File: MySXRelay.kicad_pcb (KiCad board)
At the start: 2 copper layers, 50 parts, among them K2 FH44L-1AT-L1-DC5V, Q1 2N7002, U1 MIC4427, U2 BL0942, U3 BP2525X, U4 Si8642BB-B-IS1

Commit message: finished schematic
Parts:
- C1, C13, C14: footprint Capacitor_SMD:C_0603_1608Metric -> Capacitor_SMD:C_0402_1005Metric
- C5: value 4.7u/400V -> 2.2u/400V; footprint Capacitor_THT:CP_Radial_D10.0mm_P5.00mm -> Capacitor_THT:CP_Radial_D8.0mm_P3.50mm
- C6: value 680u/10V -> 470u/10V
- L1: value 330m/300mA -> 330u; footprint Inductor_THT:L_Radial_D7.0mm_P3.00mm -> Inductor_SMD:L_1812_4532Metric_Pad1.30x3.40mm_HandSolder
- TH1: value 50mA -> ERF-LX005V2
- X1: moved to B.Cu
- moved X1 2.16 mm to (110.0, 65.0), turned to 180 degrees
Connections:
- X1 pad 1: VCC -> VRAW
- X1 pad 10: D3_INT -> D4_INT
- X1 pad 11: D6_PWM -> D5_PWM
- X1 pad 12: D5_PWM -> D6_PWM
- X1 pad 13: D8_SDA -> D7_SCL
- X1 pad 14: D7_SCL -> D8_SDA
- X1 pad 15: D10_A4 -> D9_A3
- X1 pad 16: D9_A3 -> D10_A4
- X1 pad 17: D12_MISO_RX -> D11_MOSI_TX
- X1 pad 18: D11_MOSI_TX -> D12_MISO_RX
- X1 pad 19: D14_CS -> D13_SCK
- X1 pad 2: VRAW -> VCC
- X1 pad 20: D13_SCK -> D14_CS
- X1 pad 3: GND -> VCCIO
- X1 pad 4: VCCIO -> GND
- X1 pad 5: D2_RX -> D1_TX
- X1 pad 6: D1_TX -> D2_RX
- X1 pad 7: LEGACY_ID -> RST
- X1 pad 8: RST -> LEGACY_ID
- X1 pad 9: D4_INT -> D3_INT

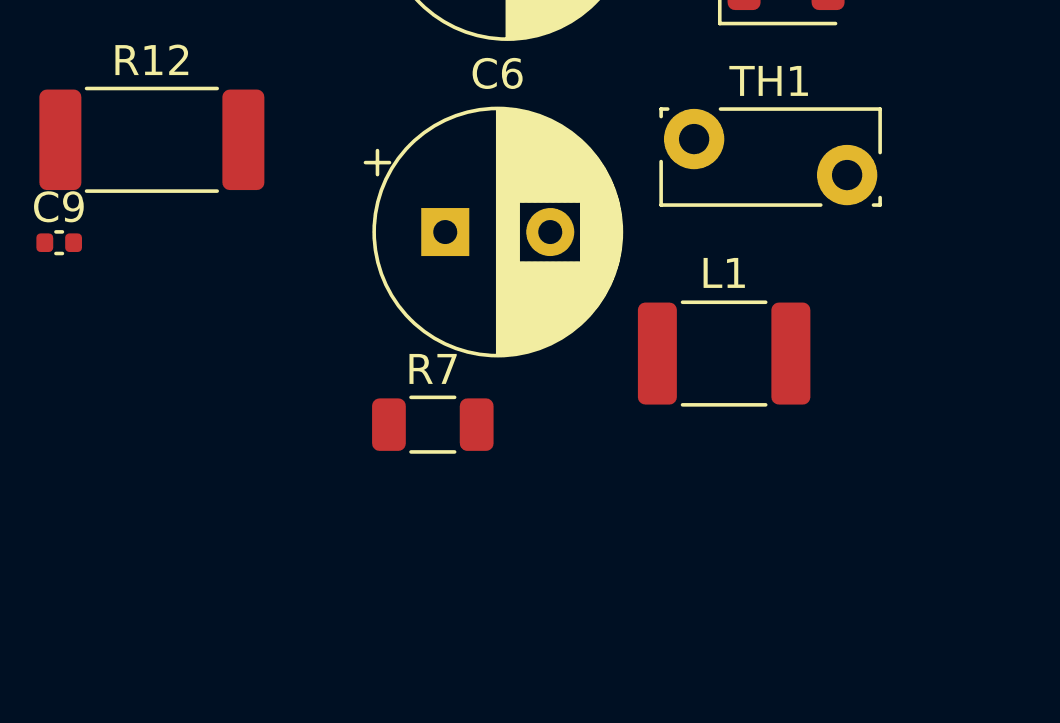
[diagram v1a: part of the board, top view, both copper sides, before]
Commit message: add LDO on mains power supply output
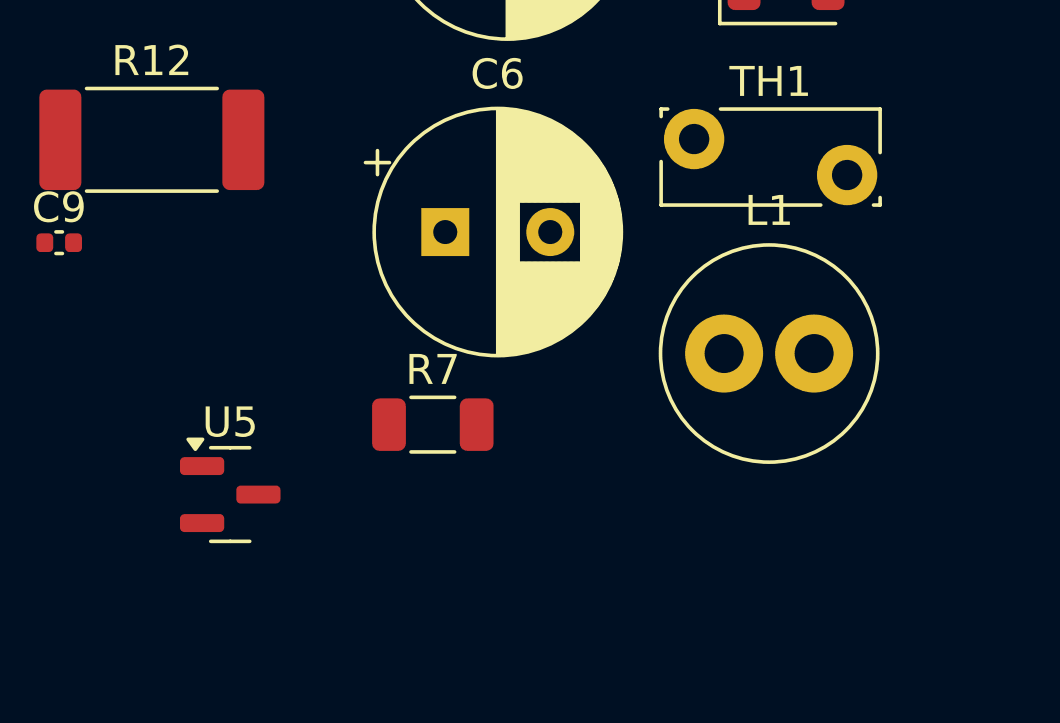
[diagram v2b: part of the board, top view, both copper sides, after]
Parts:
- added U5: MCP1703Ax-180xxTT, Package_TO_SOT_SMD:SOT-23, F.Cu at (118.2, 129.4)
- L1: footprint Inductor_SMD:L_1812_4532Metric_Pad1.30x3.40mm_HandSolder -> Inductor_THT:L_Radial_D7.0mm_P3.00mm
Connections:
- C6 pad 1: +3V3 -> Net-(U5-VI)
- L1 pad 2: +3V3 -> Net-(U5-VI)
- R8 pad 2: +3V3 -> Net-(U5-VI)
- R9 pad 1: +3V3 -> Net-(U5-VI)
- U3 pad 2: unconnected-(U3-SEL-Pad2) -> Net-(D6-K)

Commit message: setup PCS dimensions
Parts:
- K2, X2: moved to B.Cu
- moved K2 87.3 mm to (180.1, 125.8), turned to 90 degrees
- moved R12 54.4 mm to (166.2, 97.5)
- moved X2 50.2 mm to (176.9, 85.1), turned to -90 degrees
- moved TH1 49.0 mm to (164.3, 79.3)
- moved X1 45.9 mm to (136.8, 102.3)
- moved U4 44.8 mm to (156.1, 104.4)
- moved C5 44.6 mm to (164.4, 87.8)
- moved U2 44.0 mm to (165.4, 105.6)
- moved U1 43.7 mm to (165.6, 124.0)
- moved C6 39.5 mm to (147.3, 87.8)
- moved L1 37.5 mm to (155.8, 93.7)
- moved X3 37.4 mm to (143.8, 123.9)
- moved U3 33.0 mm to (158.1, 85.5)
- moved D7 21.5 mm to (132.8, 91.6)
- moved D5 14.8 mm to (138.6, 91.3)
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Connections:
- X2 pad 1: L_OUT -> N_IN
- X2 pad 2: L_IN -> N_OUT
- X2 pad 3: N_OUT -> L_IN
- X2 pad 4: N_IN -> L_OUT
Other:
- board outline added: 46.2 x 45.1 mm

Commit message: WIP
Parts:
- removed K2: FH44L-1AT-L1-DC5V, Relay_THT:Relay_SPST_Panasonic_ADW11
- added K1: FH44L-1AT-L1-DC5V, MySXRelay:RELAY-TH_FH44L-1AT-L1-DC5V, B.Cu at (172.0, 87.8)
- C5, C6, C7, D6, D7, L1, R7, R8, TH1: moved to B.Cu
- X2: footprint TerminalBlock_Phoenix:TerminalBlock_Phoenix_MKDS-1,5-4-5.08_1x04_P5.08mm_Horizontal -> MySXRelay:MSTB_2,5_4-G
- moved D1 48.1 mm to (158.1, 108.1)
- moved D2 48.1 mm to (158.1, 112.7)
- moved D3 48.1 mm to (158.1, 117.3)
- moved Q1 48.1 mm to (158.1, 122.0)
- moved C1 48.1 mm to (153.6, 106.9)
- moved C2 48.1 mm to (153.6, 109.5)
- moved R1 48.1 mm to (153.6, 112.0)
- moved R2 48.1 mm to (153.6, 114.5)
- moved R3 48.1 mm to (153.6, 117.0)
- moved R4 48.1 mm to (153.6, 119.5)
- moved R5 48.1 mm to (153.6, 122.0)
- moved R6 48.1 mm to (153.6, 124.5)
- moved U2 47.9 mm to (125.8, 78.7), turned to 90 degrees
- moved C9 43.5 mm to (152.3, 103.3)
- moved C11 43.5 mm to (143.2, 103.7)
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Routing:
- net L_OUT: track 0.00 -> 17.1 mm
- net Net-(D2-COM): track 0.00 -> 7.72 mm
- net Net-(D6-K): track 0.00 -> 5.40 mm
- net L_IN: track 0.00 -> 5.16 mm
- net Net-(D7-K): track 0.00 -> 3.64 mm
- net Net-(D7-A): track 0.00 -> 1.90 mm
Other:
- board size 46.2 x 45.1 mm -> 47.2 x 45.1 mm

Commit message: PCB WIP
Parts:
- C1, C10, C11, C12, C13, C14, C2, C3, C4, C8, C9, D1, D2, D3, D4, Q1, R1, R10, R11, R13, R2, R3, R4, R5, R6, R9, U1, U2, U3, U4, U5: moved to B.Cu
- moved C3 46.9 mm to (166.1, 123.9)
- moved C8 44.1 mm to (181.2, 121.2), turned to 90 degrees
- moved R9 40.1 mm to (178.2, 118.9)
- moved R18 36.0 mm to (169.8, 83.6), turned to 180 degrees
- moved R13 35.1 mm to (148.3, 84.0), turned to -90 degrees
- moved R17 30.6 mm to (165.2, 83.6), turned to 180 degrees
- moved U5 29.9 mm to (178.4, 121.3), turned to 180 degrees
- moved R7 26.5 mm to (178.2, 97.2), turned to 90 degrees
- moved R16 25.4 mm to (160.6, 83.6), turned to 180 degrees
- moved U2 25.4 mm to (148.1, 90.7), turned to 0 degrees
- moved L1 25.2 mm to (178.8, 104.2)
- moved R10 25.2 mm to (157.7, 93.2), turned to -90 degrees
- moved U4 25.0 mm to (150.1, 100.5), turned to -90 degrees
- moved R11 24.9 mm to (152.8, 93.3), turned to -90 degrees
- moved D6 24.7 mm to (179.2, 100.8), turned to 0 degrees
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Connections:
- D3 pad 2: VCCIO -> VCC
- D4 pad 1: VCCIO -> VCC
- K1 pad 13: L_IN -> L_OUT
- K1 pad 14: L_OUT -> L_IN
- X1 pad 3: VCCIO -> VCC
- X2 pad 3: L_IN -> L_OUT
- X2 pad 4: L_OUT -> L_IN
- X3 pad 1: VCCIO -> VCC
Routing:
- net GND: track 0.00 -> 104.3 mm
- net VCC: track 0.00 -> 68.1 mm, vias 0 -> 3
- net D5_PWM: track 0.00 -> 37.2 mm, vias 0 -> 2
- net D11_MOSI_TX: track 0.00 -> 29.1 mm, vias 0 -> 1
- net SW: track 0.00 -> 24.2 mm, vias 0 -> 1
- net D12_MISO_RX: track 0.00 -> 24.0 mm, vias 0 -> 1
- net Net-(D1-COM): track 0.00 -> 21.3 mm, vias 0 -> 2
- net D3_INT: track 0.00 -> 17.6 mm, vias 0 -> 1
- net LED: track 0.00 -> 13.6 mm
- net L_OUT: track 17.1 -> 6.76 mm
- net D4_INT: track 0.00 -> 9.18 mm
- net N_IN: track 0.00 -> 6.84 mm, vias 0 -> 1
- net Net-(Q1-G): track 0.00 -> 6.08 mm
- net Net-(D6-K): track 5.40 -> 0.00 mm
- net Net-(U1-IN_B): track 0.00 -> 5.13 mm
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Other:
- outline, holes or cut-outs redrawn

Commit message: WIP PCB
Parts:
- moved R11 5.86 mm to (158.7, 92.9)
- moved R10 4.86 mm to (152.8, 92.9)
- moved C5 1.17 mm to (176.4, 89.1)
- moved D5 1.17 mm to (178.5, 86.8)
- moved C9 0.58 mm to (144.7, 87.4), turned to 90 degrees
- moved C11 0.57 mm to (157.2, 95.2)
- moved C10 0.45 mm to (153.9, 95.2)
- moved C13 0.33 mm to (145.9, 96.3)
- turned R12 to 180 degrees
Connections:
- X2 pad 1: N_IN -> N_OUT
- X2 pad 2: N_OUT -> N_IN
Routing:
- net N_IN: track 6.84 -> 113.2 mm, vias 1 -> 5
- net +3V3: track 0.00 -> 69.3 mm, vias 0 -> 2
- net Net-(U5-VI): track 0.00 -> 16.3 mm
- net Net-(U2-IN): track 0.00 -> 15.1 mm
- net CF1: track 0.00 -> 12.5 mm
- net Net-(D6-K): track 0.00 -> 10.9 mm
- net Net-(U2-IP): track 0.00 -> 10.2 mm
- net Net-(D5-K): track 0.00 -> 10.1 mm, vias 0 -> 1
- net L_IN: track 4.30 -> 12.8 mm
- net Net-(U2-VP): track 0.00 -> 8.00 mm, vias 0 -> 1
- net RX: track 0.00 -> 6.15 mm
- net TX: track 0.00 -> 6.04 mm
- net Net-(D7-K): track 0.00 -> 3.78 mm
- net Net-(D7-A): track 0.00 -> 3.17 mm
- net Net-(D5-A): track 0.00 -> 2.52 mm
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- added copper zone on B.Cu, net Net-(D5-K)
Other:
- outline, holes or cut-outs redrawn

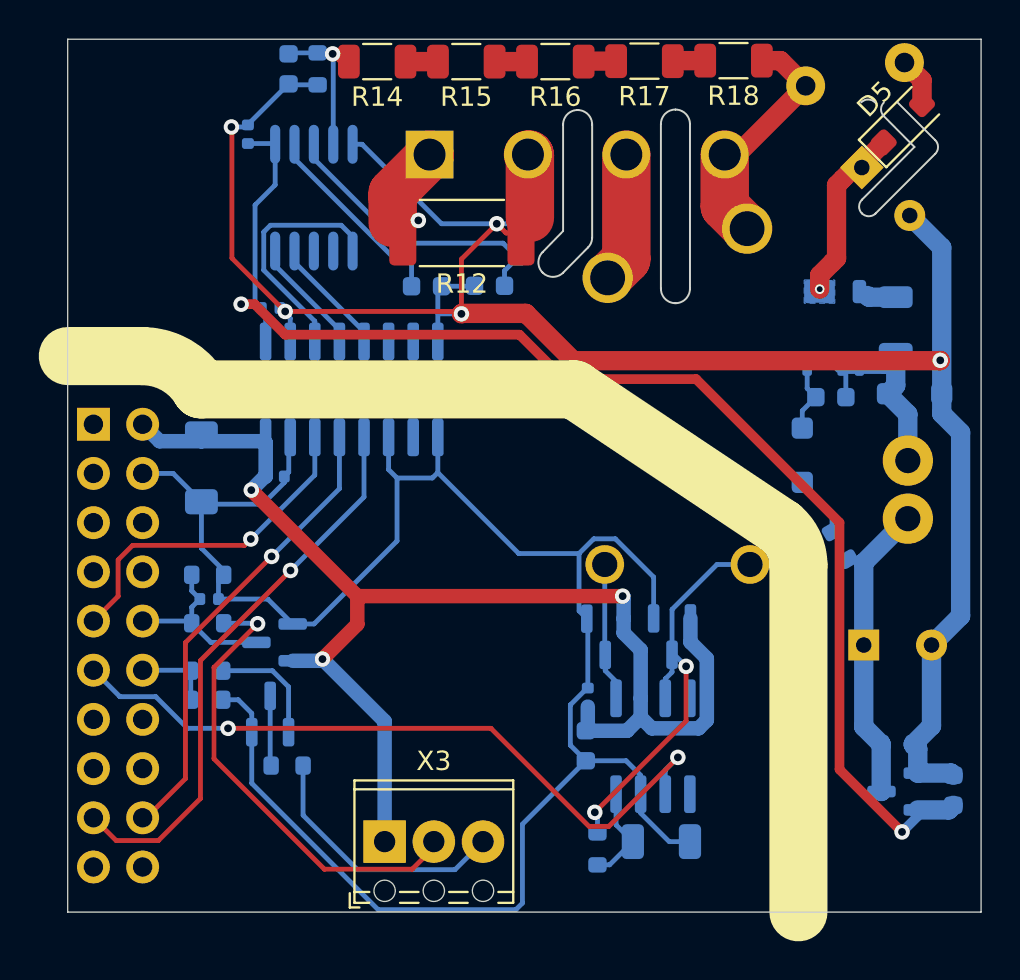
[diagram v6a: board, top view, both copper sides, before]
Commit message: PCB placment and routing finished
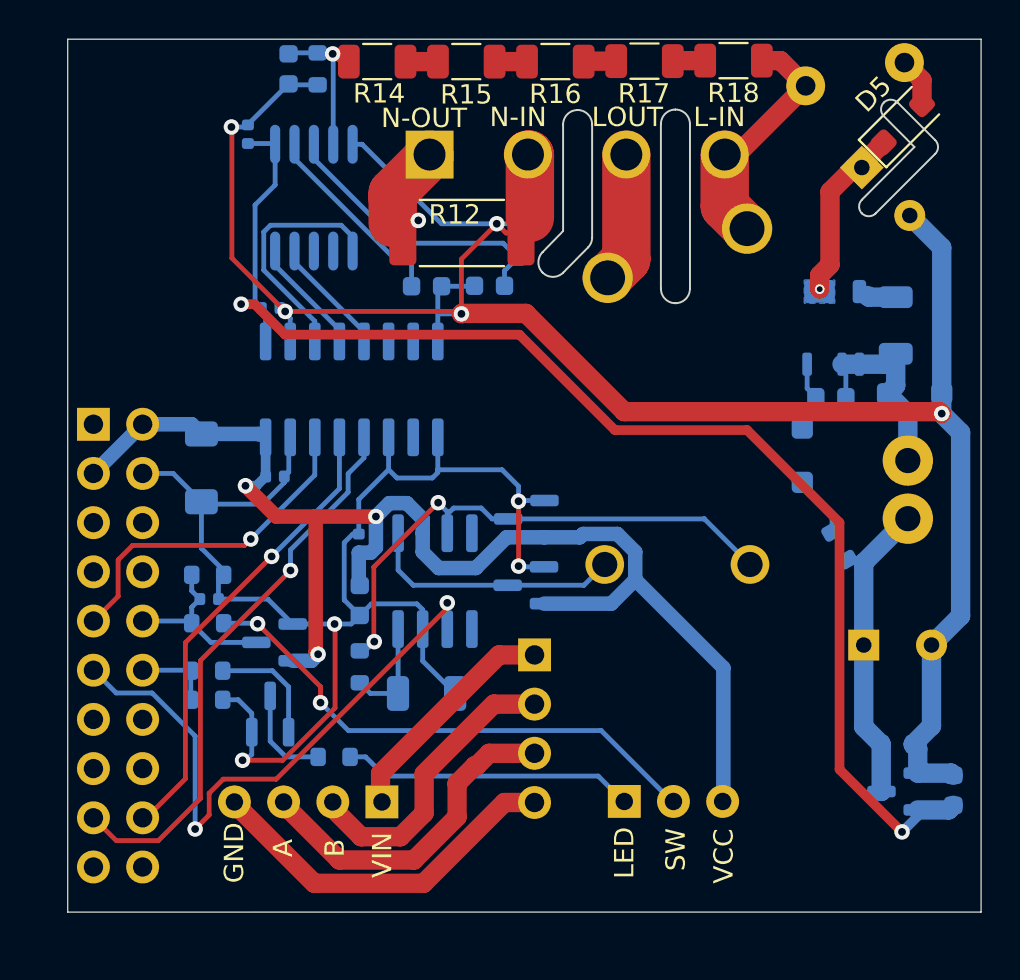
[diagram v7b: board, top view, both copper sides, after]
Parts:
- added X4: ~, Connector_PinSocket_2.54mm:PinSocket_1x04_P2.54mm_Vertical, B.Cu at (159.5, 114.3)
- added X5: ~, MySXRelay:JST-XH_S_4P-2.54MM-PIN1-RIGHT, B.Cu at (154.2, 121.9)
- X3: footprint TerminalBlock_Phoenix:TerminalBlock_Phoenix_MPT-0,5-3-2.54_1x03_P2.54mm_Horizontal -> MySXRelay:JST-XH_S_3P-2.54MM; moved to B.Cu
- moved R1 15.5 mm to (150.5, 114.9)
- moved X3 15.1 mm to (166.7, 121.8), turned to -90 degrees
- moved C3 14.3 mm to (153.9, 116.2)
- moved C1 14.2 mm to (150.4, 108.5)
- moved U1 14.1 mm to (154.4, 110.5)
- moved C2 13.9 mm to (150.5, 111.5)
- moved D1 9.67 mm to (159.1, 107.2), turned to 180 degrees
- moved D2 4.89 mm to (159.1, 110.7), turned to 180 degrees
- moved R5 2.47 mm to (149.2, 119.5)
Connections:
- X3 pad 1: VCC -> LED
- X3 pad 3: LED -> VCC
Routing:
- net GND: track 104.3 -> 74.3 mm, vias 0 -> 4
- net Net-(X4-Pin_4): track 0.00 -> 18.9 mm
- net Net-(X4-Pin_3): track 0.00 -> 17.4 mm
- net Net-(X4-Pin_2): track 0.00 -> 15.3 mm
- net Net-(X4-Pin_1): track 0.00 -> 12.1 mm
- net Net-(D1-COM): track 21.3 -> 29.2 mm
- net Net-(D2-COM): track 7.15 -> 13.3 mm
- net D5_PWM: track 37.2 -> 31.7 mm
- net SW: track 24.2 -> 27.7 mm, vias 1 -> 2
- net VCC: track 68.1 -> 71.1 mm
- net LED: track 13.6 -> 15.3 mm
- net Net-(Q1-D): track 3.62 -> 5.15 mm
- net N_IN: track 113.2 -> 114.4 mm
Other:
- outline, holes or cut-outs redrawn
- board text added: "A"
- board text added: "B"
- board text added: "GND"
- board text added: "L-IN"
- board text added: "LED"
- board text added: "LOUT"
- board text added: "N-IN"
- board text added: "N-OUT"
- board text added: "SW"
- board text added: "VCC"
- board text added: "VIN"

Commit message: version 1.0
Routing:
- added copper zone on B.Cu, net GND
- added copper zone on F.Cu, net GND
- added copper zone on B.Cu, net N_IN
- added copper zone on F.Cu, net N_IN
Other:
- board text added: "HIGH VOLTAGE !!!"
- board text added: "MySXRelay v1.0"
